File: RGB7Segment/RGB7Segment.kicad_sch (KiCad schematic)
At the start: 21 parts, among them J1 Conn_01x02_Socket, J2 Conn_01x02_Socket

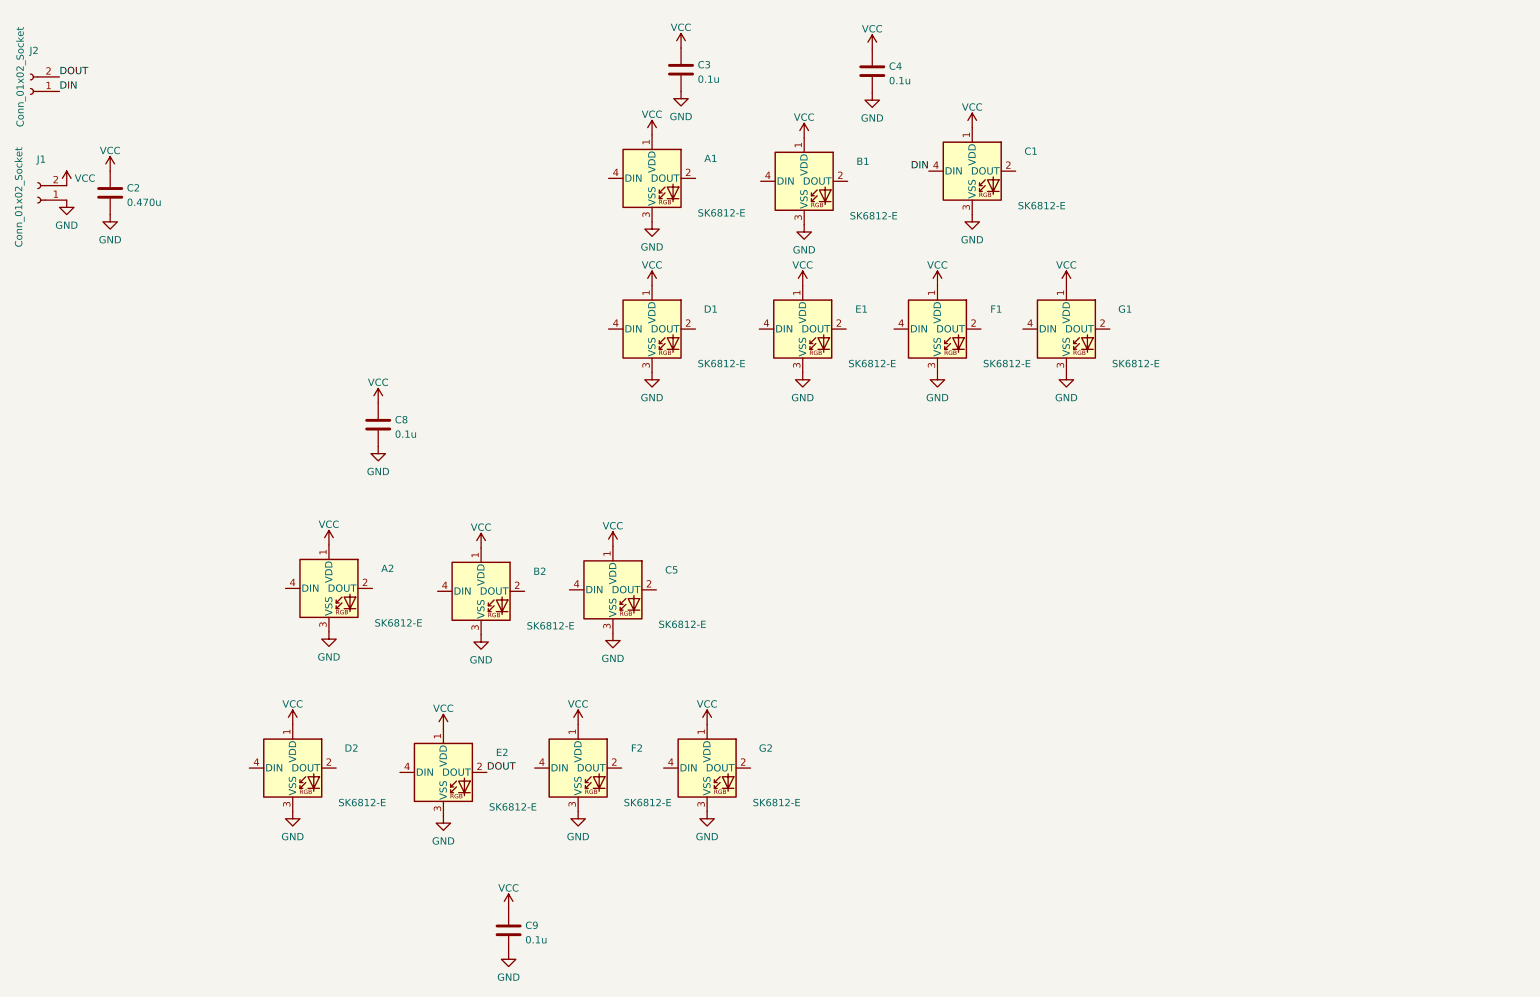
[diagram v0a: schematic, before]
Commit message: Adding base parts / positioning.
Needs further alignment for horizontal vs Verticle SKU
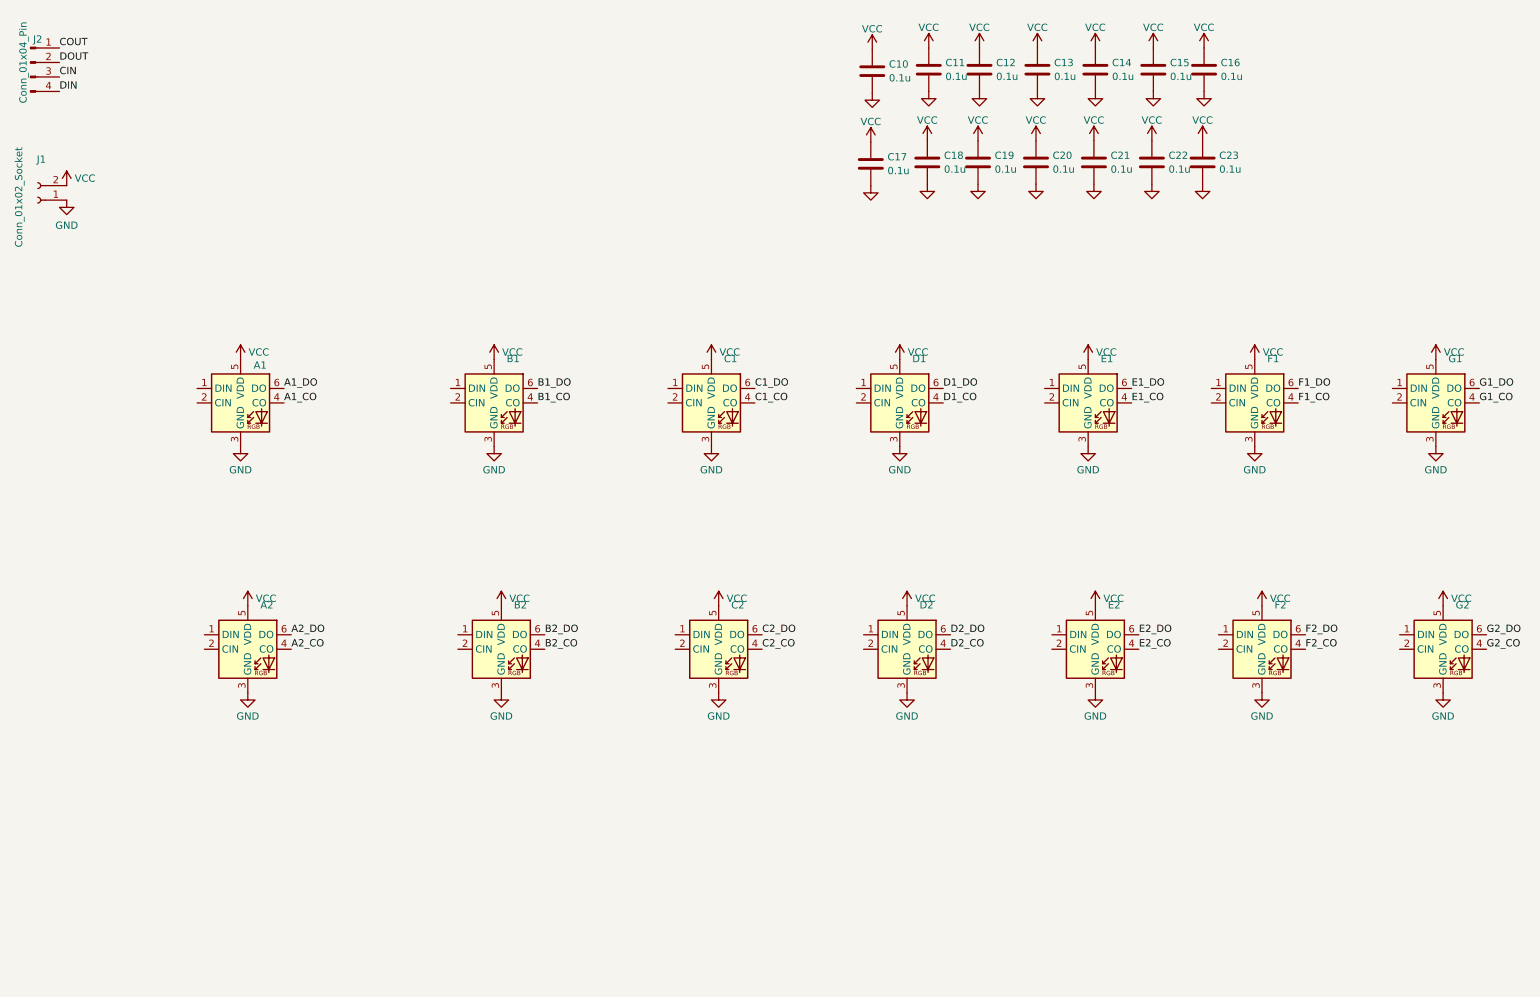
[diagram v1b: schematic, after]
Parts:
- removed A1, A2, B1, B2, C1, C5, D1, D2, E1, E2, F1, F2, G1, G2: SK6812-E, Library:4960_Test4, symbol LED:WS2812B
- removed C2: 0.470u, Capacitor_SMD:C_0402_1005Metric, symbol Device:C
- removed C3, C8, C9: 0.1u, Capacitor_SMD:C_0402_1005Metric, symbol Device:C
- removed J2: Conn_01x02_Socket, Connector_PinHeader_2.54mm:PinHeader_1x02_P2.54mm_Vertical, symbol Connector:Conn_01x02_Socket
- added A1, A2, B1, B2, C1, C2, D1, D2, E1, E2, F1, F2, G1, G2: ~, Library:587-2086-247F, symbol New_Library:Dialight_587
- added C11, C12, C13, C14, C15, C16, C17, C18, C19, C20, C21, C22, C23: 0.1u, Capacitor_SMD:C_0402_1005Metric, symbol Device:C
- added J2: Conn_01x04_Pin, Connector_PinHeader_1.27mm:PinHeader_1x04_P1.27mm_Vertical_SMD_Pin1Left, symbol Connector:Conn_01x04_Pin
- J1: footprint Connector_PinHeader_2.54mm:PinHeader_1x02_P2.54mm_Vertical -> Connector_PinHeader_1.27mm:PinHeader_1x02_P1.27mm_Vertical_SMD_Pin1Left
- renumbered C4 to C10
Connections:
- net DIN: now also J2.4 (Pin_4)
- net DOUT: now also J2.2 (Pin_2)
- net GND: now also A1.3 (GND), A2.3 (GND), B1.3 (GND), B2.3 (GND), C1.3 (GND), C11.2, C12.2, C13.2, C14.2, C15.2, C16.2, C17.2, C18.2, C19.2, C2.3 (GND), C20.2, C21.2, C22.2, C23.2, D1.3 (GND), D2.3 (GND), E1.3 (GND), E2.3 (GND), F1.3 (GND), F2.3 (GND), G1.3 (GND), G2.3 (GND)
- net VCC: now also A1.5 (VDD), A2.5 (VDD), B1.5 (VDD), B2.5 (VDD), C1.5 (VDD), C11.1, C12.1, C13.1, C14.1, C15.1, C16.1, C17.1, C18.1, C19.1, C2.5 (VDD), C20.1, C21.1, C22.1, C23.1, D1.5 (VDD), D2.5 (VDD), E1.5 (VDD), E2.5 (VDD), F1.5 (VDD), F2.5 (VDD), G1.5 (VDD), G2.5 (VDD)
- new net A1_CO: A1.4 (CO)
- new net A1_DO: A1.6 (DO)
- new net A2_CO: A2.4 (CO)
- new net A2_DO: A2.6 (DO)
- new net B1_CO: B1.4 (CO)
- new net B1_DO: B1.6 (DO)
- new net B2_CO: B2.4 (CO)
- new net B2_DO: B2.6 (DO)
- new net C1_CO: C1.4 (CO)
- new net C1_DO: C1.6 (DO)
- new net C2_CO: C2.4 (CO)
- new net C2_DO: C2.6 (DO)
- new net CIN: J2.3 (Pin_3)
- new net COUT: J2.1 (Pin_1)
- new net D1_CO: D1.4 (CO)
- new net D1_DO: D1.6 (DO)
- new net D2_CO: D2.4 (CO)
- new net D2_DO: D2.6 (DO)
- new net E1_CO: E1.4 (CO)
- new net E1_DO: E1.6 (DO)
- new net E2_CO: E2.4 (CO)
- new net E2_DO: E2.6 (DO)
- new net F1_CO: F1.4 (CO)
- new net F1_DO: F1.6 (DO)
- new net F2_CO: F2.4 (CO)
- new net F2_DO: F2.6 (DO)
- new net G1_CO: G1.4 (CO)
- new net G1_DO: G1.6 (DO)
- new net G2_CO: G2.4 (CO)
- new net G2_DO: G2.6 (DO)

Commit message: Initial Horizontal Placement
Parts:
- J1: footprint Connector_PinHeader_1.27mm:PinHeader_1x02_P1.27mm_Vertical_SMD_Pin1Left -> Connector_PinHeader_1.27mm:PinHeader_1x02_P1.27mm_Vertical
- J2: footprint Connector_PinHeader_1.27mm:PinHeader_1x04_P1.27mm_Vertical_SMD_Pin1Left -> Connector_PinHeader_1.27mm:PinHeader_1x04_P1.27mm_Vertical
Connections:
- net E1_CO is gone; now on net COUT: E1.4 (CO)
- net E1_DO is gone; now on net DOUT: E1.6 (DO)
- net A1_CO: now also B1.2 (CIN)
- net A1_DO: now also B1.1 (DIN)
- net A2_CO: now also G2.2 (CIN)
- net A2_DO: now also G2.1 (DIN)
- net B1_CO: now also F2.2 (CIN)
- net B1_DO: now also F2.1 (DIN)
- net B2_CO: now also C2.2 (CIN)
- net B2_DO: now also C2.1 (DIN)
- net C1_CO: now also D1.2 (CIN)
- net C1_DO: now also D1.1 (DIN)
- net C2_CO: now also D2.2 (CIN)
- net C2_DO: now also D2.1 (DIN)
- net CIN: now also F1.2 (CIN)
- net COUT: now also J2.2 (Pin_2); no longer J2.1 (Pin_1)
- net D1_CO: now also E1.2 (CIN)
- net D1_DO: now also E1.1 (DIN)
- net D2_CO: now also E2.2 (CIN)
- net D2_DO: now also E2.1 (DIN)
- net DIN: now also F1.1 (DIN)
- net DOUT: now also J2.1 (Pin_1); no longer J2.2 (Pin_2)
- net E2_CO: now also C1.2 (CIN)
- net E2_DO: now also C1.1 (DIN)
- net F1_CO: now also G1.2 (CIN)
- net F1_DO: now also G1.1 (DIN)
- net F2_CO: now also A2.2 (CIN)
- net F2_DO: now also A2.1 (DIN)
- net G1_CO: now also A1.2 (CIN)
- net G1_DO: now also A1.1 (DIN)
- net G2_CO: now also B2.2 (CIN)
- net G2_DO: now also B2.1 (DIN)
